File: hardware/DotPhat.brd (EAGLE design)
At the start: 30 x 65 mm, 23 parts, among them CN1 1X4-BIG, J2 RASPBERRYPI-40-PIN-GPIO_PTH, J3 USB-MICROB, U1 ATMEGA328P-MU-QFN32, X3 S4B-ZR

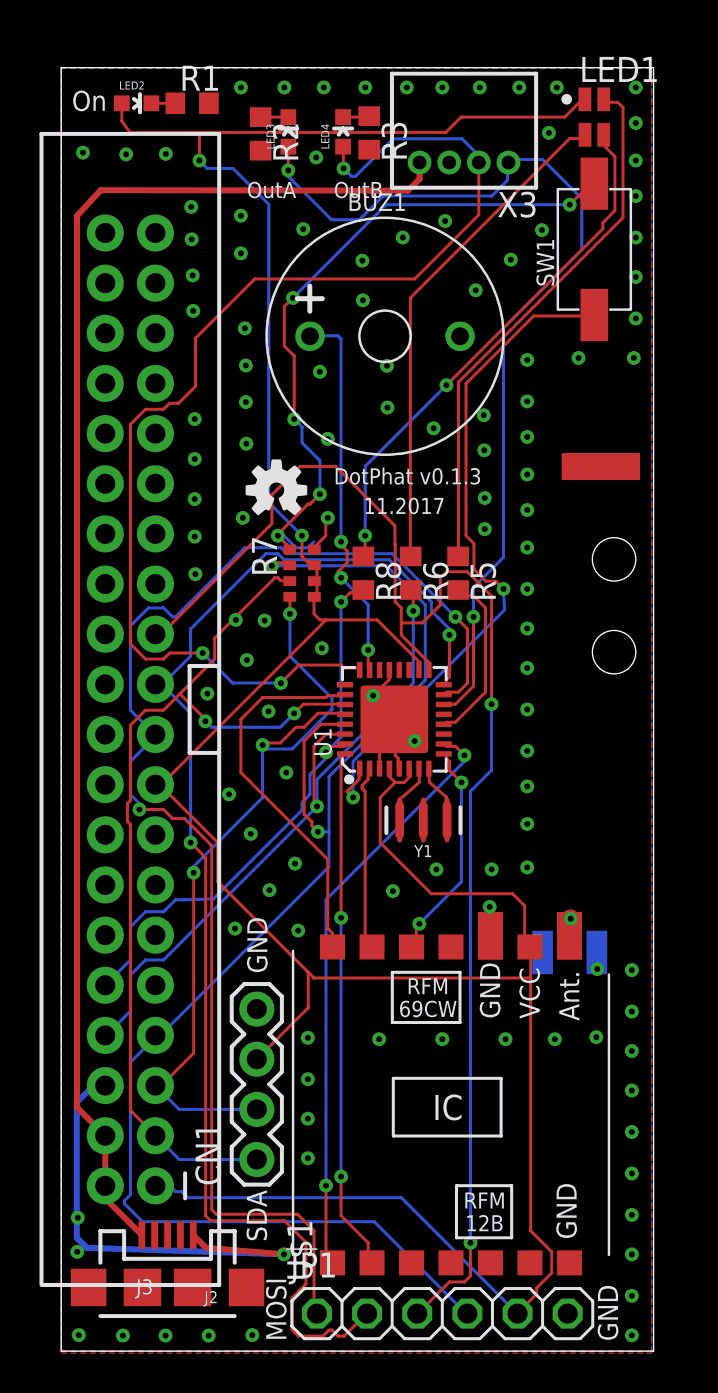
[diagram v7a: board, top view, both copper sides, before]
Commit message: Add radio led
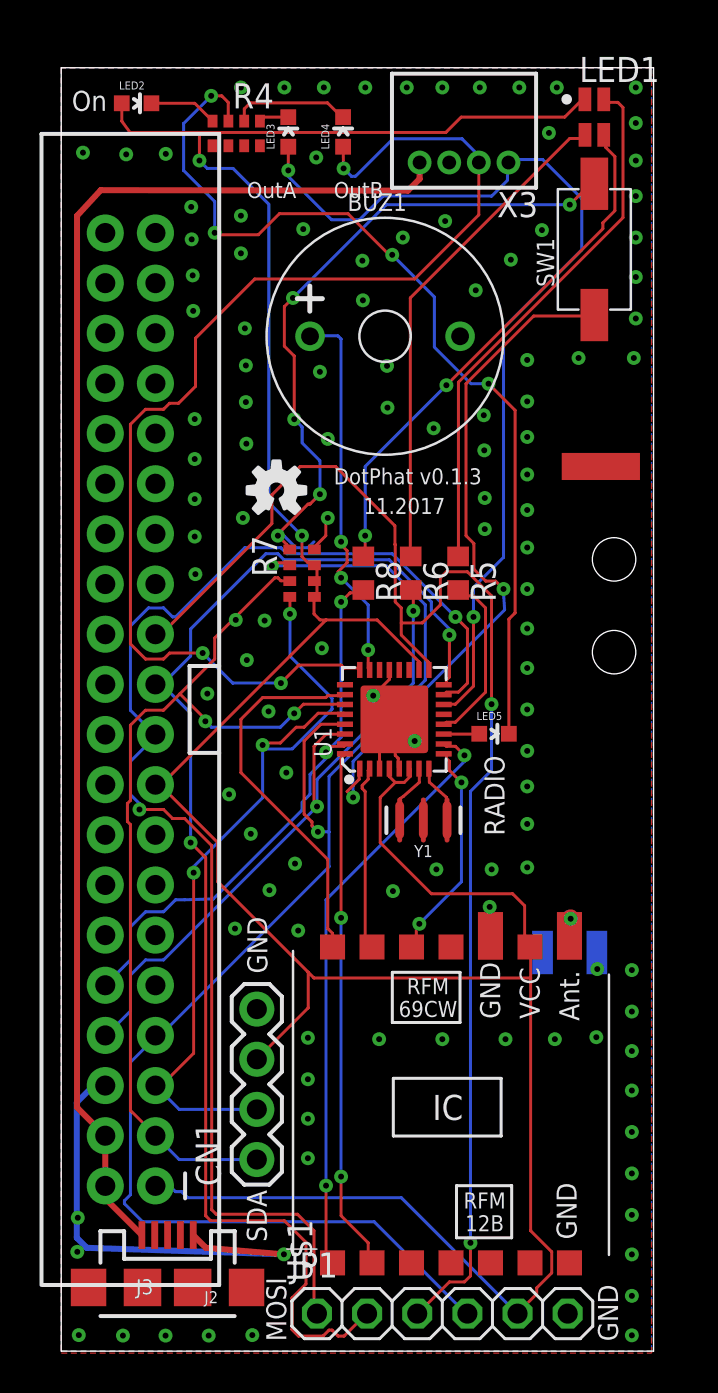
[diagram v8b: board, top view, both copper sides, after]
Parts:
- removed R1, R2, R3: 250Ω, resistor:R0603
- added LED5: (no value), SparkFun:LED-0603
- added R4: 150Ω, SparkFun:0603-ARV
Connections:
- removed net LIGHT_SENSE_ENA: U1.11
- new net N$10: LED5.C, R4.3
- new net RADIO_ON: LED5.A, U1.11
- net GND: now also R4.5, R4.6, R4.7, R4.8; no longer R1.2, R2.2, R3.2
- net N$2: now also LED3.C, R4.1; no longer LED2.C, R1.1
- net N$7: now also LED2.C, R4.4; no longer LED3.C, R2.1
- net N$9: now also R4.2; no longer R3.1
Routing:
- net N$10: track 0.00 -> 47.9 mm, vias 0 -> 4
- net N$9: track 1.36 -> 6.05 mm
- net N$7: track 1.40 -> 3.47 mm
- net RADIO_ON: track 0.00 -> 1.81 mm
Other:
- board text added: "RADIO"
